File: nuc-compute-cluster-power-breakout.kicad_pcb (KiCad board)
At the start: 4 copper layers, 100 x 100 mm, 136 parts, among them J1 USB3106-30-0230-A, J10 10107844-002LF, J2 BM04B-SRSS-TB-LF-SN, J3 BM04B-SRSS-TB-LF-SN, J4 43045-1013, J5 430450812, J6 430450812, J7 430450812, J8 430450812, J9 430450812, Q1 SQS401EN-T1_BE3, Q10 SSM3K15ACT, Q11 BC856,215, Q15 DMN4010LFG-7, Q2 SQS401EN-T1_BE3, Q3 SSM3K15ACT, Q4 SSM3K15ACT, Q5 SQS401EN-T1_BE3, Q6 SSM3K15ACT, Q7 SQS401EN-T1_BE3, Q8 SQS401EN-T1_BE3, Q9 SSM3K15ACT, U1 FT2232HL-REEL, U10 TCA9534, U11 TMCS1100A2-Q1, U12 TMCS1100A2-Q1, U13 TMCS1100A2-Q1, U14 ADS7828, U15 AP62301WU-7, U7 AP62301WU-7, U8 TMCS1100A2-Q1, U9 TMCS1100A2-Q1, Y1 KX-7_12,MHz

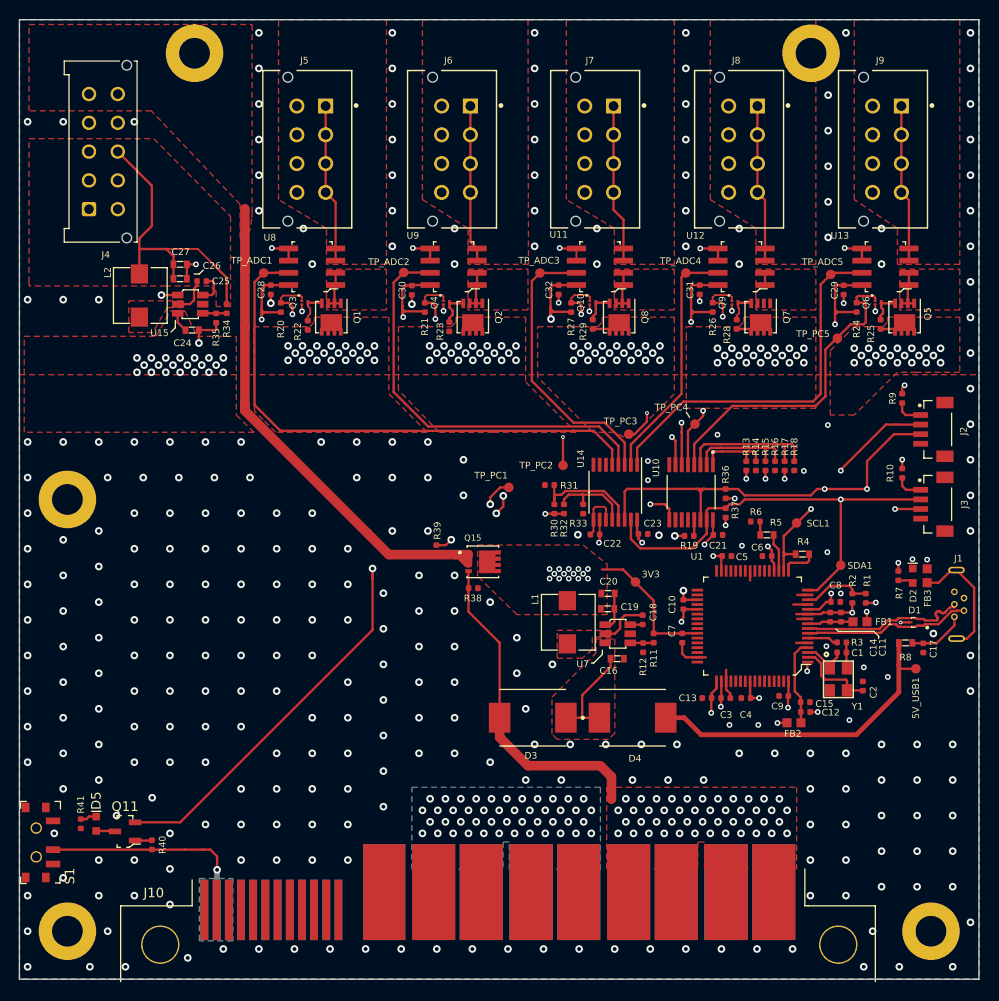
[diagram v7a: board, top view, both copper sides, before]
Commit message: Adjust the power plane distribution
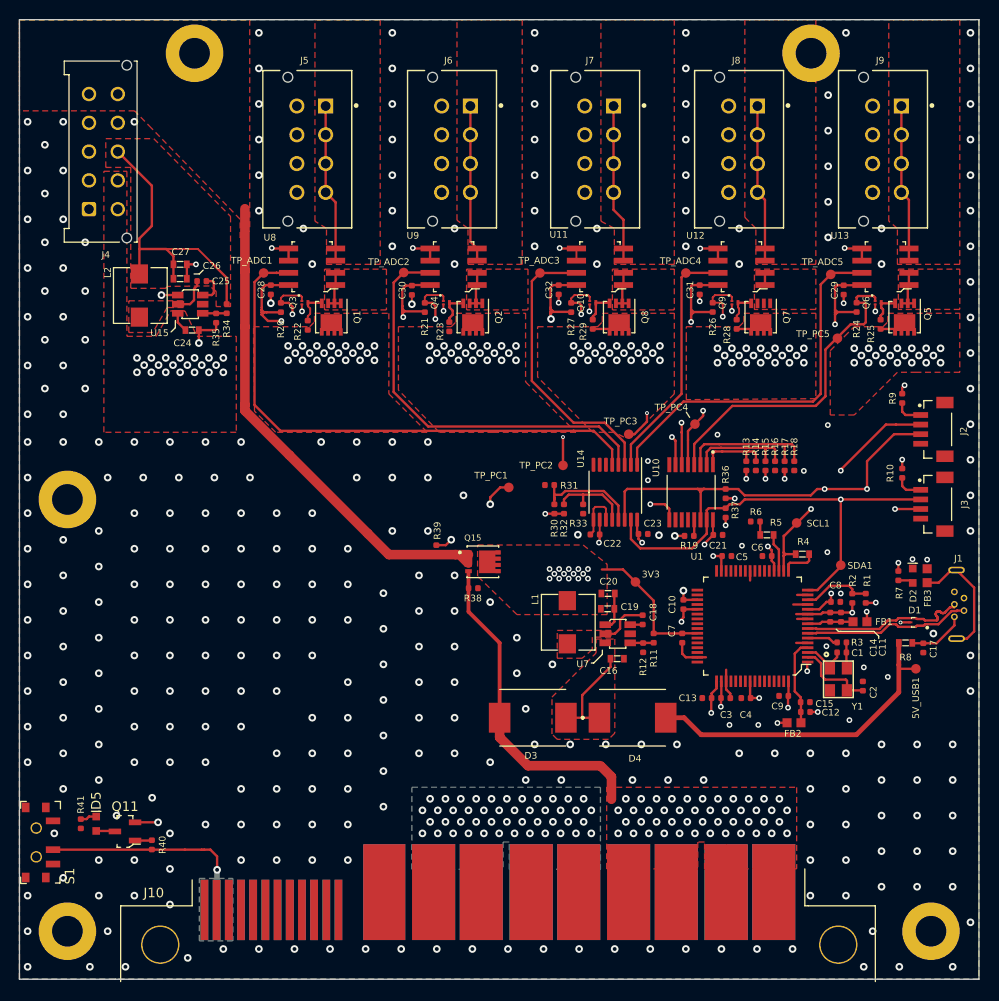
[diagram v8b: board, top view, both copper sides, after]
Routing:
- net VCC3V3: track 247.3 -> 239.9 mm, vias 44 -> 42
- net /Power Cycling & Current Measurement/PC_1: track 67.7 -> 61.2 mm
- net GND: vias 367 -> 381
- net (no net): vias 0 -> 4
